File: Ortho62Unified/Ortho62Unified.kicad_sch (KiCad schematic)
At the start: 178 parts, among them J1 AVR-PDI-6, J2 Conn_01x06_Socket, J3 USB_C_Receptacle_USB2.0, J4 Conn_01x08_Socket, J5 Conn_01x06_Socket, SW1 SW_Push, SW10 SW_Push, SW11 SW_Push, SW12 SW_Push, SW13 SW_Push, SW14 SW_Push, SW15 SW_Push, SW16 SW_Push, SW17 SW_Push, SW18 SW_Push, SW19 SW_Push, SW2 SW_Push, SW20 SW_Push, SW21 SW_Push, SW22 SW_Push, SW23 SW_Push, SW24 SW_Push, SW25 SW_Push, SW26 SW_Push, SW27 SW_Push, SW28 SW_Push, SW29 SW_Push, SW3 SW_Push, SW30 SW_Push, SW31 SW_Push, SW32 SW_Push, SW33 SW_Push, SW34 SW_Push, SW35 SW_Push, SW36 SW_Push, SW37 SW_Push, SW38 SW_Push, SW39 SW_Push, SW4 SW_Push, SW40 SW_Push, SW41 SW_Push, SW42 SW_Push, SW43 SW_Push, SW44 SW_Push, SW45 SW_Push, SW46 SW_Push, SW47 SW_Push, SW48 SW_Push, SW49 SW_Push, SW5 SW_Push, SW50 SW_Push, SW51 SW_Push, SW52 SW_Push, SW53 SW_Push, SW54 SW_Push, SW55 SW_Push, SW56 SW_Push, SW57 SW_Push, SW58 SW_Push, SW59 SW_Push, SW6 SW_Push, SW60 SW_Push, SW61 SW_Push, SW62 SW_Push, SW63 SW_Push, SW64 SW_Push, SW65 SW_Push, SW66 SW_Push, SW67 SW_Push, SW68 SW_Push, SW69 SW_Push, SW7 SW_Push, SW70 SW_Push, SW71 SW_Push, SW72 SW_Push, SW73 SW_Push, SW75 SW_Push, SW78 SW_Push, SW79 SW_Push, SW8 SW_Push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

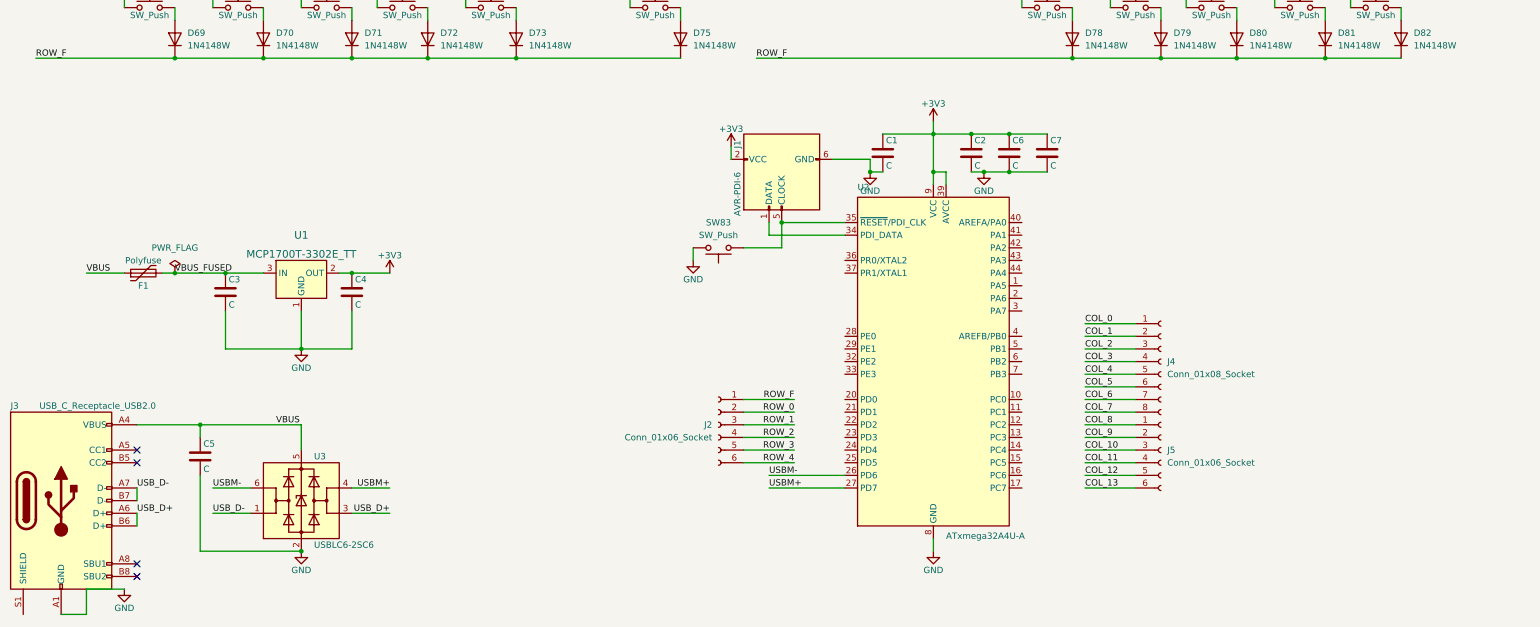
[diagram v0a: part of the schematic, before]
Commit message: Progress routing rows and columns.
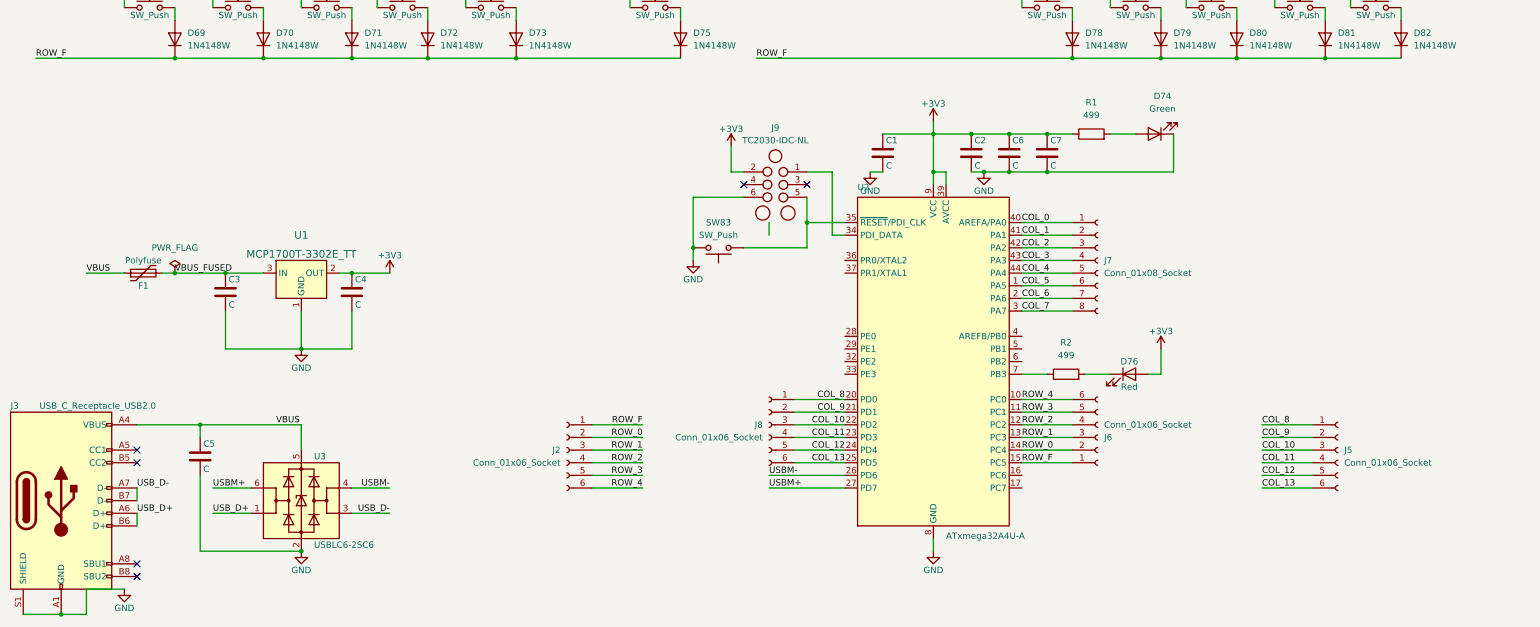
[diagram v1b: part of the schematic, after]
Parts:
- removed J1: AVR-PDI-6, Connector_PinHeader_2.54mm:PinHeader_2x03_P2.54mm_Horizontal, symbol Connector:AVR-PDI-6
- removed J4: Conn_01x08_Socket, Connector_PinHeader_1.27mm:PinHeader_1x08_P1.27mm_Vertical, symbol Connector:Conn_01x08_Socket
- added D74: Green, LED_SMD:LED_0805_2012Metric_Pad1.15x1.40mm_HandSolder, symbol Device:LED
- added D76: Red, LED_SMD:LED_0805_2012Metric_Pad1.15x1.40mm_HandSolder, symbol Device:LED
- added J6, J8: Conn_01x06_Socket, Connector_PinHeader_1.27mm:PinHeader_1x06_P1.27mm_Vertical, symbol Connector:Conn_01x06_Socket
- added J7: Conn_01x08_Socket, Connector_PinHeader_1.27mm:PinHeader_1x08_P1.27mm_Vertical, symbol Connector:Conn_01x08_Socket
- added J9: TC2030-IDC-NL, Tag_Connect:TC2030-IDC-NL, symbol Tag-Connect:TC2030-IDC-NL
- added R1: 499, Resistor_SMD:R_0805_2012Metric_Pad1.20x1.40mm_HandSolder, symbol Device:R
- added R2: 499, LED_SMD:LED_0805_2012Metric_Pad1.15x1.40mm_HandSolder, symbol Device:R
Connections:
- net +3V3: now also D76.2 (A), J9.2 (Pin_2), R1.1
- net COL_0: now also U2.40 (AREFA/PA0), J7.1 (Pin_1)
- net COL_1: now also U2.41 (PA1), J7.2 (Pin_2)
- net COL_10: now also U2.22 (PD2), J8.3 (Pin_3)
- net COL_11: now also U2.23 (PD3), J8.4 (Pin_4)
- net COL_12: now also U2.24 (PD4), J8.5 (Pin_5)
- net COL_13: now also U2.25 (PD5), J8.6 (Pin_6)
- net COL_2: now also U2.42 (PA2), J7.3 (Pin_3)
- net COL_3: now also U2.43 (PA3), J7.4 (Pin_4)
- net COL_4: now also U2.44 (PA4), J7.5 (Pin_5)
- net COL_5: now also U2.1 (PA5), J7.6 (Pin_6)
- net COL_6: now also U2.2 (PA6), J7.7 (Pin_7)
- net COL_7: now also U2.3 (PA7), J7.8 (Pin_8)
- net COL_8: now also U2.20 (PD0), J8.1 (Pin_1)
- net COL_9: now also U2.21 (PD1), J8.2 (Pin_2)
- net GND: now also J3.S1 (SHIELD), D74.1 (K), J9.6 (Pin_6)
- net ROW_0: now also U2.14 (PC4), J6.2 (Pin_2)
- net ROW_1: now also U2.13 (PC3), J6.3 (Pin_3)
- net ROW_2: now also U2.12 (PC2), J6.4 (Pin_4)
- net ROW_3: now also U2.11 (PC1), J6.5 (Pin_5)
- net ROW_4: now also U2.10 (PC0), J6.6 (Pin_6)
- net ROW_F: now also U2.15 (PC5), J6.1 (Pin_1)
- net USBM+: now also U3.6 (I/O1); no longer U3.4 (I/O2)
- net USBM-: now also U3.4 (I/O2); no longer U3.6 (I/O1)
- net USB_D+: now also U3.1 (I/O1); no longer U3.3 (I/O2)
- net USB_D-: now also U3.3 (I/O2); no longer U3.1 (I/O1)
- net at U2.34 (PDI_DATA): now also J9.1 (Pin_1)
- net at SW83.1, U2.35 (~{RESET}/PDI_CLK): now also J9.5 (Pin_5)
- net at U2.7 (PB3): now also R2.1
- new net: D76.1 (K), R2.2
- new net: D74.2 (A), R1.2
- no-connect marks 4 -> 6
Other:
- moved on the sheet: J2, J5

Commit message: Routing complete for Xmega based design.
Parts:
- U1: footprint digikey-footprints:SOT-23-3 -> Package_TO_SOT_SMD:SOT-23-3
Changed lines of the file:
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@@
       (effects (font (size 1.524 1.524)))
     )
-    (property "Footprint" "digikey-footprints:SOT-23-3" (at 81.28 210.82 0)
+    (property "Footprint" "Package_TO_SOT_SMD:SOT-23-3" (at 81.28 210.82 0)
       (effects (font (size 1.524 1.524)) (justify left) hide)
     )

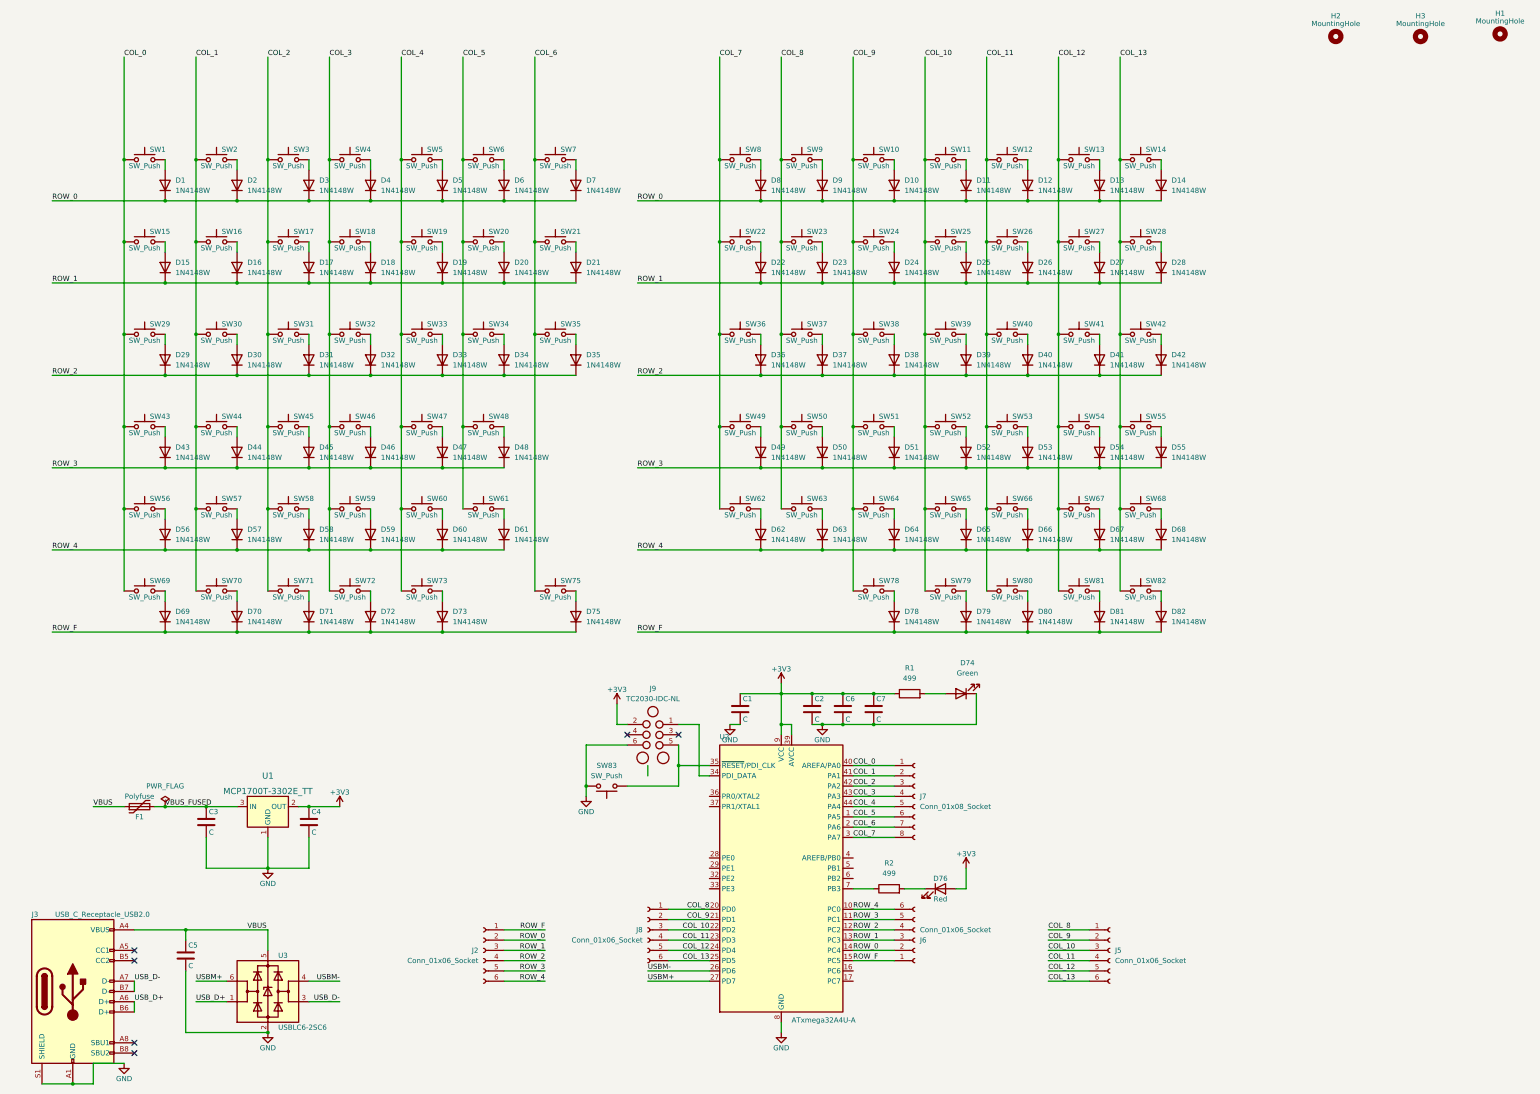
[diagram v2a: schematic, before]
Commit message: Add additional key in bottom row.
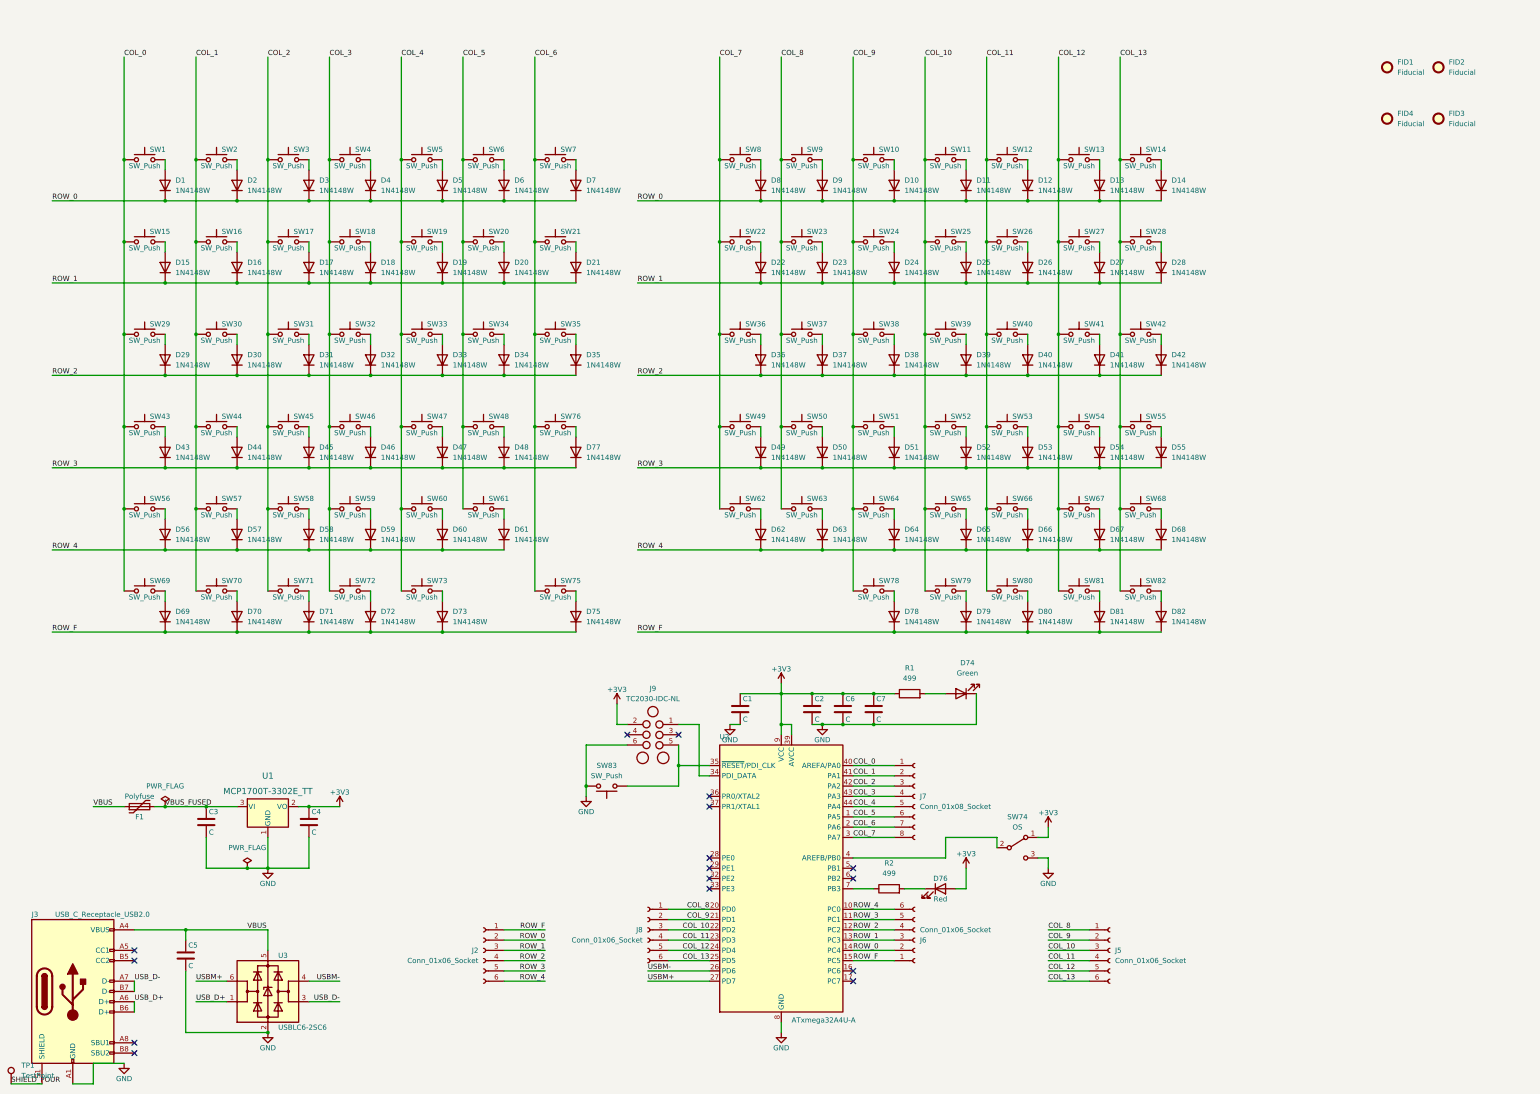
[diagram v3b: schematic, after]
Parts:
- removed H1, H2, H3: MountingHole, MountingHole:MountingHole_3.2mm_M3, symbol Mechanical:MountingHole
- added D77: 1N4148W, Diode_SMD:D_SOD-123, symbol Diode:1N4148W
- added FID1, FID2, FID3, FID4: Fiducial, Fiducial:Fiducial_0.5mm_Mask1mm, symbol Mechanical:Fiducial
- added SW74: OS, Button_Switch_SMD:SW_SPDT_CK-JS102011SAQN, symbol Switch:SW_SPDT
- added SW76: SW_Push, Switch_Keyboard_Kailh:SW_Kailh_Choc_V1V2_1.00u, symbol Switch:SW_Push
- added TP1: TestPoint, TestPoint:TestPoint_Pad_D1.0mm, symbol Connector:TestPoint
- U1: footprint Package_TO_SOT_SMD:SOT-23-3 -> Package_TO_SOT_SMD:SOT-23; symbol dk_PMIC-Voltage-Regulators-Linear:MCP1700T-3302E_TT -> Regulator_Linear:MCP1700x-330xxTT
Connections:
- net +3V3: now also SW74.1 (A)
- net COL_6: now also SW76.1
- net GND: now also SW74.3 (C); no longer J3.S1 (SHIELD)
- net ROW_3: now also D77.1 (K)
- net at U2.4 (AREFB/PB0): now also SW74.2 (B)
- new net: D77.2 (A), SW76.2
- new net SHIELD_POUR: J3.S1 (SHIELD), TP1.1
- no-connect marks 6 -> 16

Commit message: Makes bottom row with modifier keys symmetric.
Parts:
- SW62: footprint Switch_Keyboard_Kailh:SW_Kailh_Choc_V1V2_1.50u -> Switch_Keyboard_Kailh:SW_Kailh_Choc_V1V2_1.00u
- SW63: footprint Switch_Keyboard_Kailh:SW_Kailh_Choc_V1V2_1.00u -> Switch_Keyboard_Kailh:SW_Kailh_Choc_V1V2_1.50u
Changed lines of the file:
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@@
       (effects (font (size 1.27 1.27)))
     )
-    (property "Footprint" "Switch_Keyboard_Kailh:SW_Kailh_Choc_V1V2_1.50u" (at 193.04 137.16 0)
+    (property "Footprint" "Switch_Keyboard_Kailh:SW_Kailh_Choc_V1V2_1.00u" (at 193.04 137.16 0)
       (effects (font (size 1.27 1.27)) hide)
     )
@@
       (effects (font (size 1.27 1.27)))
     )
-    (property "Footprint" "Switch_Keyboard_Kailh:SW_Kailh_Choc_V1V2_1.00u" (at 208.28 137.16 0)
+    (property "Footprint" "Switch_Keyboard_Kailh:SW_Kailh_Choc_V1V2_1.50u" (at 208.28 137.16 0)
       (effects (font (size 1.27 1.27)) hide)
     )
